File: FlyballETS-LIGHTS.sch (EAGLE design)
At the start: 20 parts, among them IC1 74HC595N, IC2 ULN2003AN, IC3 LM555N

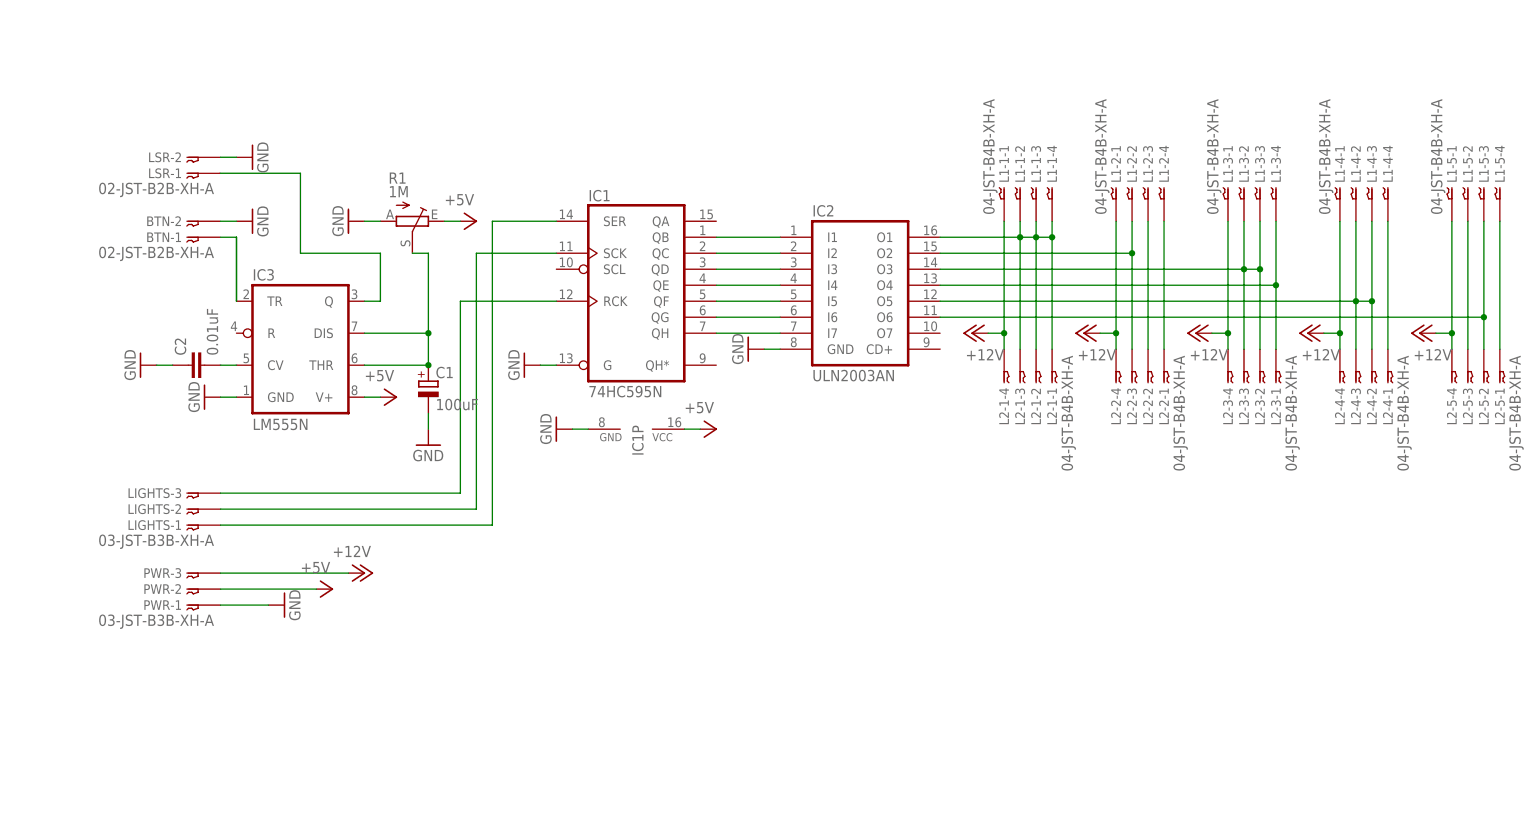
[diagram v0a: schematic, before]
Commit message: Updated drawings and added PNG exports
- Added frames around drawings to make it look neater
- Added PNG export files so people who don't have EAGLE can see
everything
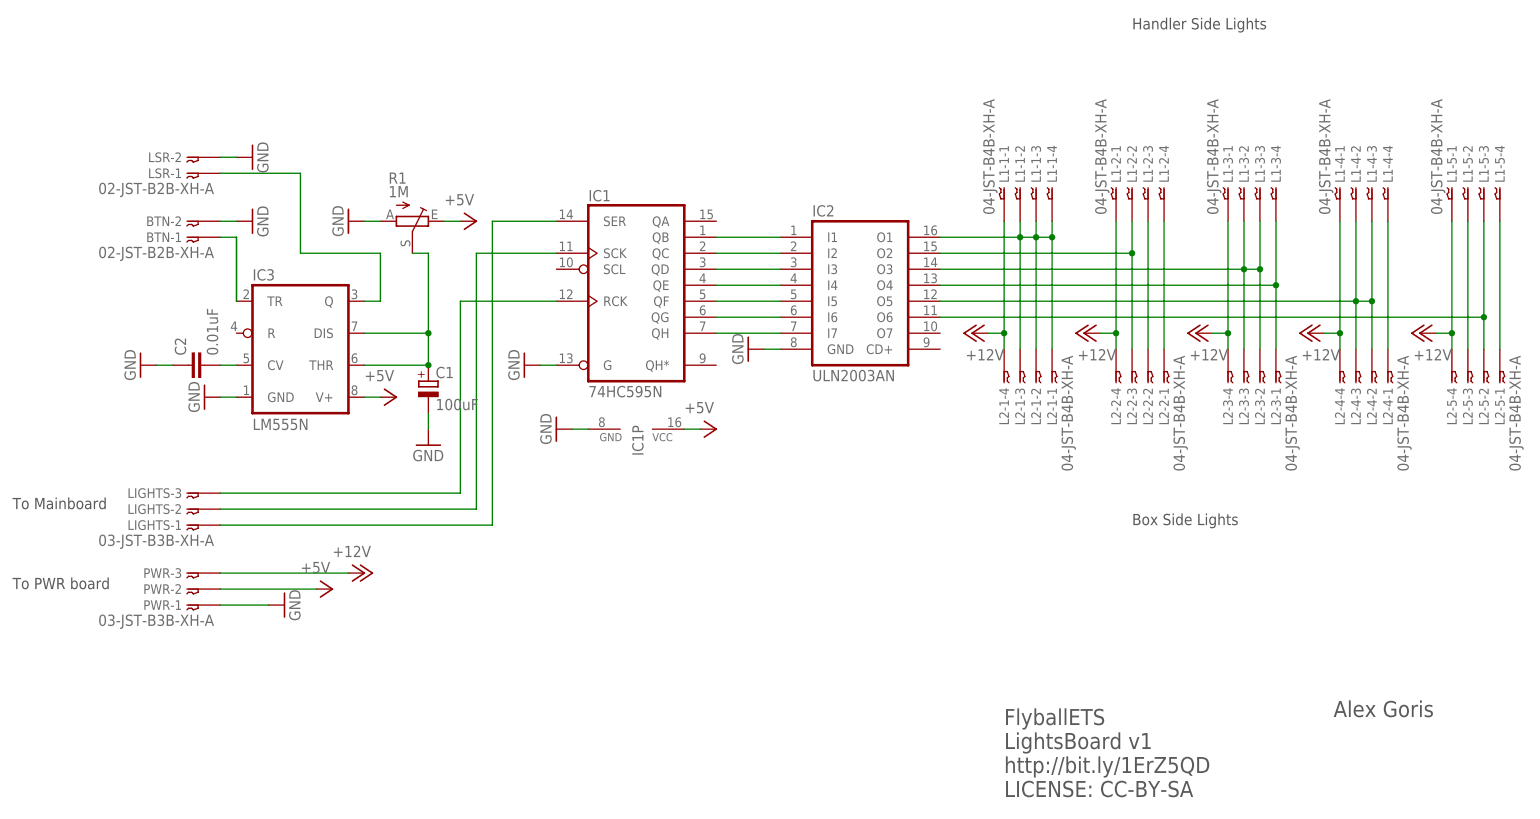
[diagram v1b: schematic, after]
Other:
- note added: "Alex Goris"
- note added: "Box Side Lights"
- note added: "FlyballETS LightsBoard v1 http://bit.ly/1ErZ5QD LICENSE: CC-BY-SA"
- note added: "Handler Side Lights"
- note added: "To Mainboard"
- note added: "To PWR board"
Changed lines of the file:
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@@
 <part name="LSR" library="bt_con-jst-xh" deviceset="02-JST" device="-B2B-XH-A"/>
 <part name="GND10" library="supply1" deviceset="GND" device=""/>
+<part name="FRAME1" library="frames" deviceset="A4L-LOC" device=""/>
 </parts>
 <sheets>
 <sheet>
 <plain>
+<text x="-17.78" y="20.32" size="1.778" layer="97">To Mainboard</text>
+<text x="-17.78" y="7.62" size="1.778" layer="97">To PWR board</text>
+<text x="160.02" y="96.52" size="1.778" layer="97">Handler Side Lights</text>
+<text x="160.02" y="17.78" size="1.778" layer="97">Box Side Lights</text>
+<text x="139.7" y="-25.4" size="2.54" layer="97">FlyballETS
+LightsBoard v1
+http://bit.ly/1ErZ5QD
+LICENSE: CC-BY-SA</text>
+<text x="192.024" y="-12.7" size="2.54" layer="97">Alex Goris</text>
 </plain>
 <instances>
@@
 <instance part="LSR" gate="-2" x="10.16" y="76.2" rot="R180"/>
 <instance part="GND10" gate="1" x="20.32" y="76.2" rot="R90"/>
+<instance part="FRAME1" gate="G$1" x="-25.4" y="-33.02"/>
 </instances>
 <busses>
@@
 </schematic>
 </drawing>
+<compatibility>
+<note version="6.3" minversion="6.2.2" severity="warning">
+Since Version 6.2.2 text objects can contain more than one line,
+which will not be processed correctly with this version.
+</note>
+</compatibility>
 </eagle>

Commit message: v2 release of remaining boards.
- Lightsboard: Corrected swapped pin connections on L2 side and made
smaller
- Powerboard: Made smaller and added descriptions for LM2596 board
- Sensorboard: Made smaller
- All boards: Removed JST connector type names
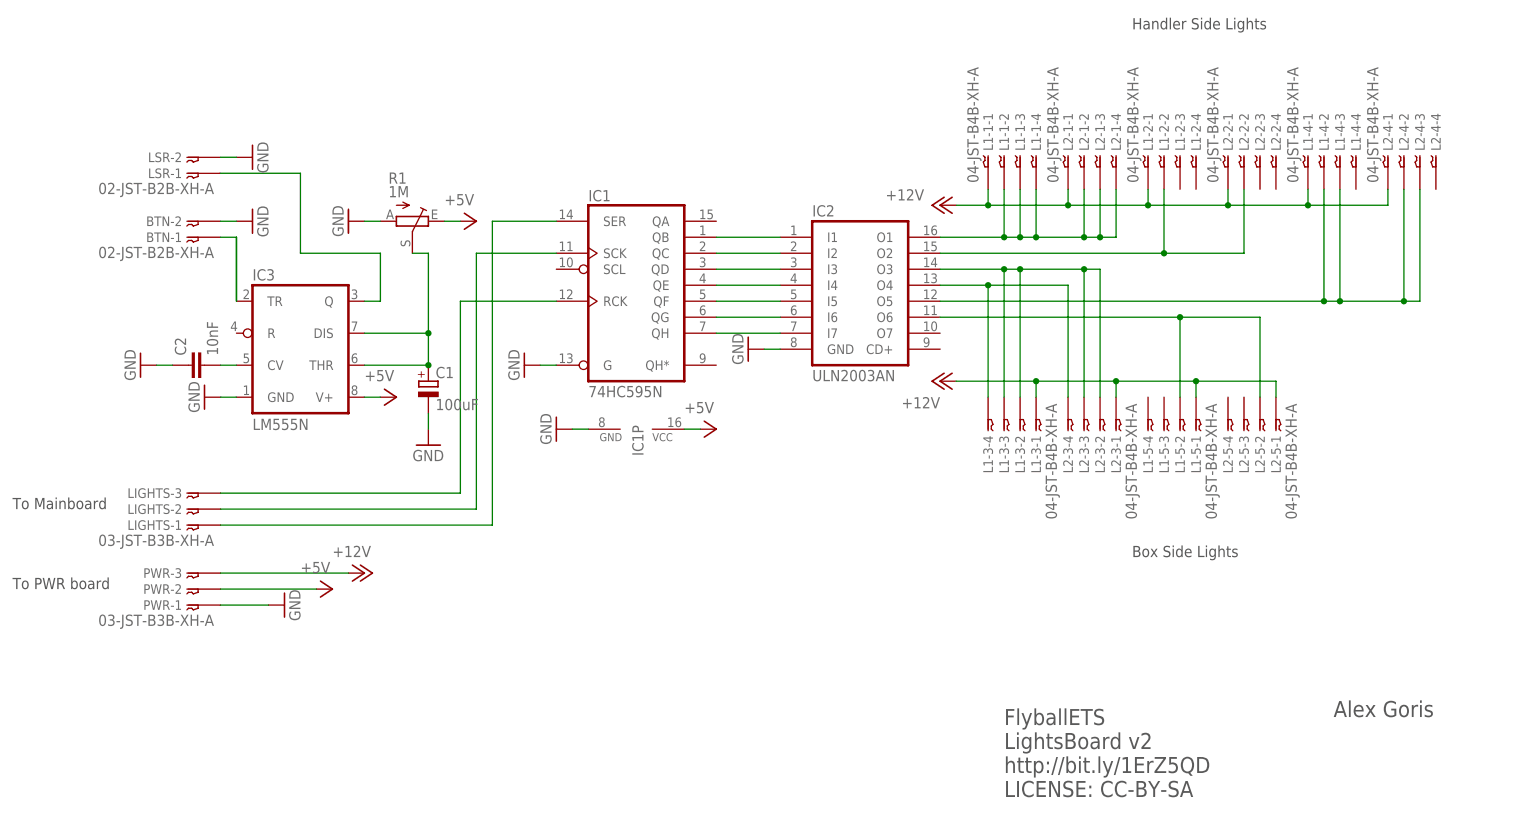
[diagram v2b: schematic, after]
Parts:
- C2: value 0.01uF -> 10nF; device resistor:C-EU025-050X050 -> resistor:C-EU050-030X075
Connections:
- removed net N$17: L1-2-3.1, L2-2-2.1
- removed net N$18: L1-2-4.1, L2-2-1.1
- removed net N$26: L1-4-4.1, L2-4-1.1
- removed net N$28: L1-5-2.1, L2-5-3.1
- removed net N$30: L1-5-4.1, L2-5-1.1
- net +12V: now also L2-1-1.1, L2-2-1.1, L2-3-1.1, L2-4-1.1, L2-5-1.1; no longer L2-1-4.1, L2-2-4.1, L2-3-4.1, L2-4-4.1, L2-5-4.1
- net N$13: now also L2-1-4.1; no longer L2-1-1.1
- net N$16: now also L2-2-2.1; no longer L2-2-3.1
- net N$22: now also L2-3-4.1; no longer L2-3-1.1
- net N$29: now also L1-5-2.1; no longer L1-5-3.1
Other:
- note added: "FlyballETS LightsBoard v2 http://bit.ly/1ErZ5QD LICENSE: CC-BY-SA"
- note removed: "FlyballETS LightsBoard v1 http://bit.ly/1ErZ5QD LICENSE: CC-BY-SA"
- moved on the sheet: L1-1-1, L1-1-2, L1-1-3, L1-1-4, L1-2-1, L1-2-2, L1-2-3, L1-2-4, L1-3-1, L1-3-2, L1-3-3, L1-3-4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

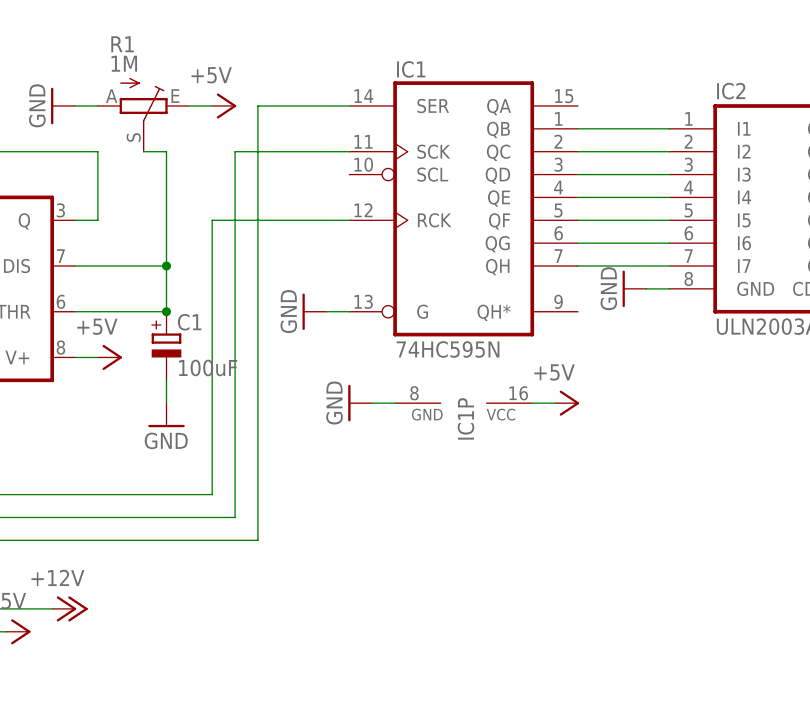
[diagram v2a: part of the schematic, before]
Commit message: LightsBoard:Fix 74HC595 problems
Closes #5
- Added decoupling capacitor over GND and VCC of 74HC595
- Added missing connection of 74HC595 pin10 to +5V
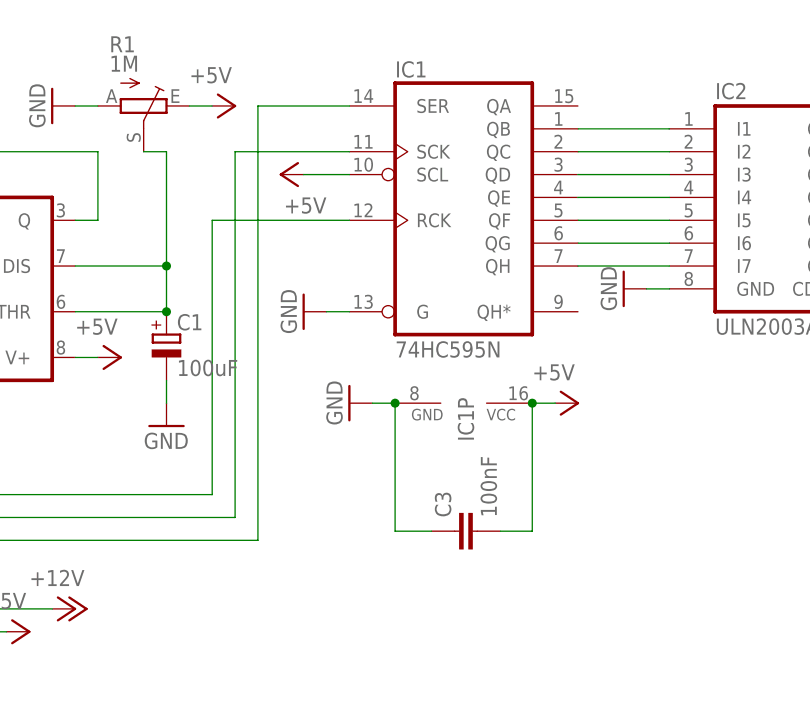
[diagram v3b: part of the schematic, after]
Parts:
- added C3: 100nF, resistor:C-EU050-030X075
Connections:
- net +5V: now also C3.2, IC1A.SCL
- net GND: now also C3.1
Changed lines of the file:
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@@
 <part name="FRAME1" library="frames" deviceset="A4L-LOC" device=""/>
 <part name="P+7" library="supply1" deviceset="+12V" device=""/>
+<part name="C3" library="resistor" deviceset="C-EU" device="050-030X075" value="100nF"/>
+<part name="P+5" library="supply1" deviceset="+5V" device=""/>
 </parts>
 <sheets>
@@
 <attribute name="VALUE" x="129.54" y="38.1" size="1.778" layer="96" rot="R180"/>
 </instance>
+<instance part="C3" gate="G$1" x="80.264" y="18.796" rot="R90"/>
+<instance part="P+5" gate="1" x="60.96" y="58.42" rot="R90"/>
 </instances>
 <busses>
@@
 <pinref part="IC1" gate="P" pin="GND"/>
 <wire x1="71.12" y1="33.02" x2="73.66" y2="33.02" width="0.1524" layer="91"/>
+<wire x1="73.66" y1="33.02" x2="73.66" y2="18.796" width="0.1524" layer="91"/>
+<junction x="73.66" y="33.02"/>
+<pinref part="C3" gate="G$1" pin="1"/>
+<wire x1="73.66" y1="18.796" x2="77.724" y2="18.796" width="0.1524" layer="91"/>
 </segment>
 <segment>
@@
 <pinref part="P+3" gate="1" pin="+5V"/>
 <wire x1="91.44" y1="33.02" x2="88.9" y2="33.02" width="0.1524" layer="91"/>
+<wire x1="88.9" y1="33.02" x2="88.9" y2="18.796" width="0.1524" layer="91"/>
+<junction x="88.9" y="33.02"/>
+<pinref part="C3" gate="G$1" pin="2"/>
+<wire x1="88.9" y1="18.796" x2="85.344" y2="18.796" width="0.1524" layer="91"/>
 </segment>
 <segment>
@@
 <wire x1="50.8" y1="66.04" x2="53.34" y2="66.04" width="0.1524" layer="91"/>
 </segment>
+<segment>
+<pinref part="P+5" gate="1" pin="+5V"/>
+<pinref part="IC1" gate="A" pin="SCL"/>
+<wire x1="63.5" y1="58.42" x2="68.58" y2="58.42" width="0.1524" layer="91"/>
+</segment>
 </net>

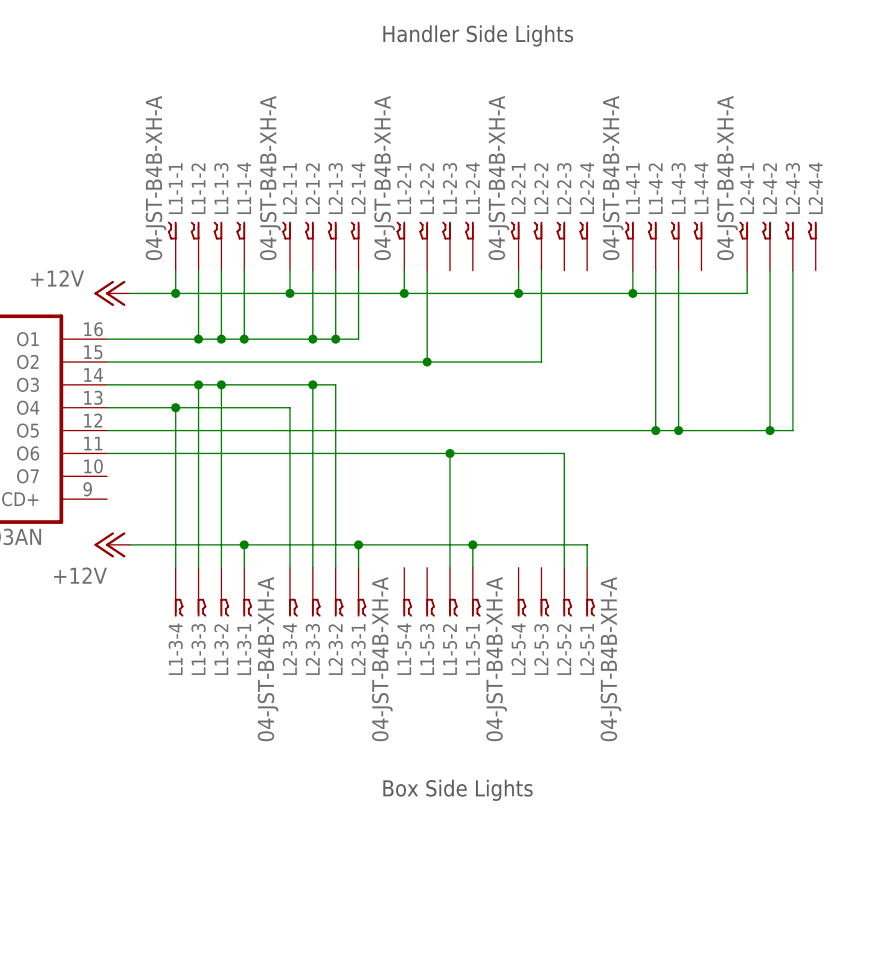
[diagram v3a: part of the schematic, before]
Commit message: Fixed several issues
- Checked all mounting holes (fixes #1 )
- Marked light colors on lights PCB (fixes #7 )
- Swapped pins 2 and 3 on LIGHTS connected on PWR board (fixes #3 )
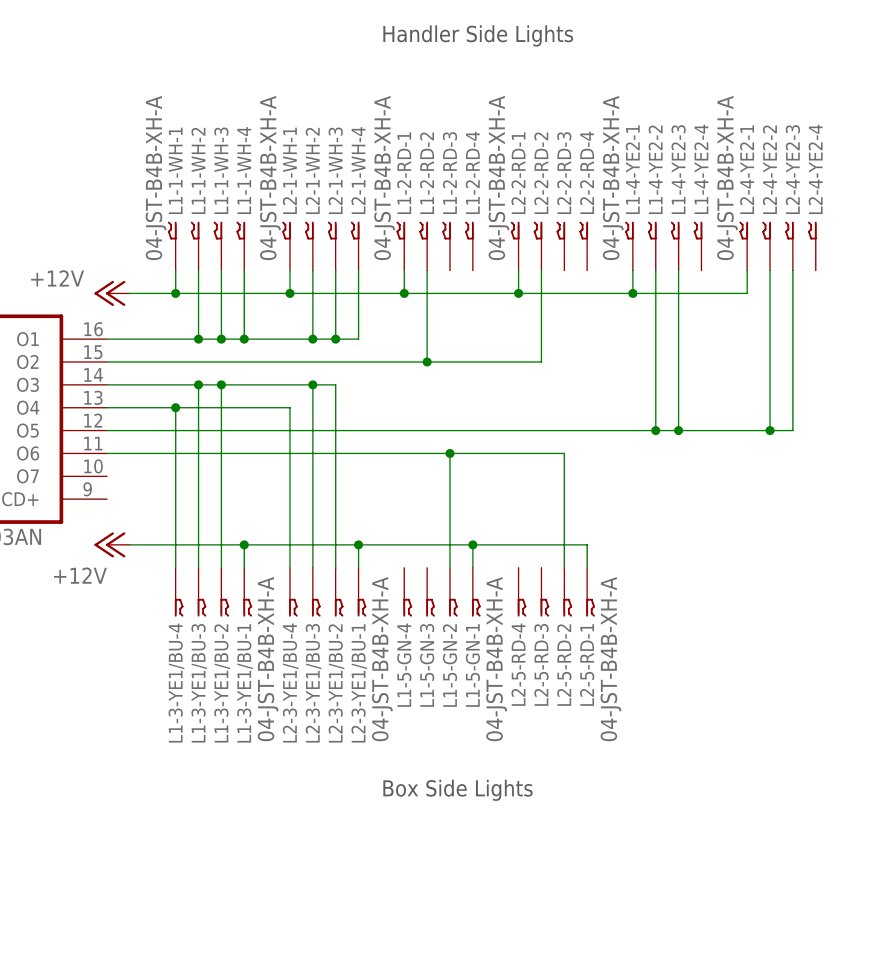
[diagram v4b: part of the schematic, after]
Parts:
- renumbered L1-1 to L1-1-WH, L1-2 to L1-2-RD, L1-3 to L1-3-YE1/BU, L1-4 to L1-4-YE2, L1-5 to L1-5-GN, L2-1 to L2-1-WH, L2-2 to L2-2-RD, L2-3 to L2-3-YE1/BU, L2-4 to L2-4-YE2, L2-5 to L2-5-RD
